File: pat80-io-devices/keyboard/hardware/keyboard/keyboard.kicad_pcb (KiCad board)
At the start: 2 copper layers, 117 parts, among them J3 Keyboard connector, SW1 1, SW10 3, SW11 E, SW12 D, SW13 C, SW14 V, SW15 F, SW16 R, SW17 4, SW18 5, SW19 T, SW2 Q, SW20 G, SW21 B, SW22 N, SW23 H, SW24 Y, SW25 6, SW26 7, SW27 U, SW28 J, SW29 M, SW3 A, SW30 ', SW31 K, SW32 I, SW33 8, SW34 9, SW35 O, SW36 L, SW37 P, SW38 [, SW39 ], SW4 Z, SW40 0, SW41 BACKSPACE, SW42 TILDE, SW43 TAB, SW44 ,, SW45 ., SW46 SPACE, SW47 /, SW48 ;, SW49 LSHIFT, SW5 X, SW50 CTRL, SW51 RSHIFT, SW52 RETURN, SW53 PATO, SW54 CAPSLK, SW6 S, SW7 W, SW8 2, SW9 CAPSLK_LED

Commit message: Fine-positioned caps lock switch
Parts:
- removed SW9: CAPSLK_LED, footprints:SW_TH_DPDT_Pushbutton_Latched
- moved R2 115.5 mm to (151.1, 20.3), turned to 90 degrees
- moved D9 39.0 mm to (34.3, 94.5), turned to 180 degrees
- moved R1 19.2 mm to (29.2, 71.1), turned to 270 degrees
- moved SW54 13.5 mm to (37.5, 69.2)
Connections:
- SW54 pad 4: (no net) -> Net-(SW54-Pad4)
- SW54 pad 5: (no net) -> GND
- SW54 pad 6: (no net) -> Net-(D9-Pad1)
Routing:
- net /ROW0: track 181.7 -> 5.46 mm
- net VCC: track 46.6 -> 50.1 mm

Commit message: Distanced keys to avoid interference
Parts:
- moved D51 8.47 mm to (252.1, 69.2)
- moved SW52 8.47 mm to (260.6, 72.0)
- moved D39 8.18 mm to (271.0, 47.9)
- moved SW39 8.18 mm to (279.5, 51.7)
- moved D36 7.85 mm to (219.7, 69.2)
- moved SW36 7.85 mm to (228.7, 72.0)
- moved SW50 7.69 mm to (226.9, 112.8)
- moved D49 7.69 mm to (218.7, 109.3)
- moved D38 7.67 mm to (251.5, 47.9)
- moved SW38 7.67 mm to (259.7, 51.7)
- moved D31 7.24 mm to (200.0, 69.2)
- moved SW31 7.24 mm to (208.8, 72.0)
- moved SW37 7.17 mm to (239.9, 51.7)
- moved D37 7.17 mm to (230.6, 47.9)
- moved D48 7.15 mm to (193.9, 109.3)
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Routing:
- net /COL0: track 120.8 -> 1.60 mm

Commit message: WIP routing keyboard
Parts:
- SW1, SW10, SW11, SW12, SW13, SW14, SW15, SW16, SW17, SW18, SW19, SW2, SW20, SW21, SW22, SW23, SW24, SW25, SW26, SW27, SW28, SW29, SW3, SW30, SW31, SW32, SW33, SW34, SW35, SW36, SW37, SW38, SW39, SW4, SW40, SW42, SW44, SW45, SW47, SW48, SW5, SW6, SW7, SW8: footprint Button_Switch_Keyboard:SW_Cherry_MX1A_1.00u_PCB -> Button_Switch_Keyboard:SW_Cherry_MX1A_1.00u_Plate
- SW43, SW50, SW53: footprint Button_Switch_Keyboard:SW_Cherry_MX1A_1.50u_PCB -> Button_Switch_Keyboard:SW_Cherry_MX1A_1.50u_Plate
- SW46, SW52: footprint Button_Switch_Keyboard:SW_Cherry_MX1A_2.25u_PCB -> Button_Switch_Keyboard:SW_Cherry_MX1A_2.25u_Plate
- SW49: footprint Button_Switch_Keyboard:SW_Cherry_MX1A_1.25u_PCB -> Button_Switch_Keyboard:SW_Cherry_MX1A_1.25u_Plate
- SW51: footprint Button_Switch_Keyboard:SW_Cherry_MX1A_1.75u_PCB -> Button_Switch_Keyboard:SW_Cherry_MX1A_1.75u_Plate
- moved R2 47.0 mm to (195.6, 5.08)
- moved C5 47.0 mm to (231.1, -1.27)
- moved R3 47.0 mm to (199.4, 5.08)
- moved R4 47.0 mm to (203.2, 5.08)
- moved R5 47.0 mm to (207.0, 5.08)
- moved R6 47.0 mm to (210.8, 5.08)
- moved R7 47.0 mm to (214.6, 5.08)
- moved R8 47.0 mm to (218.4, 5.08)
- moved R9 47.0 mm to (222.2, 5.08)
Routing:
- net /ROW0: track 5.46 -> 201.8 mm
- net /ROW7: track 9.90 -> 199.3 mm
- net /COL1: track 0.00 -> 149.9 mm, vias 0 -> 6
- net /COL2: track 0.00 -> 149.7 mm, vias 0 -> 6
- net /COL0: track 1.60 -> 151.1 mm, vias 0 -> 6
- net VCC: track 50.1 -> 0.36 mm
- net GND: track 60.3 -> 40.6 mm
- net /ROW6: track 7.88 -> 0.00 mm
- net /ROW5: track 6.61 -> 0.51 mm
- net /ROW3: track 5.26 -> 0.00 mm
- net /ROW4: track 5.79 -> 0.76 mm
- net /ROW2: track 4.74 -> 0.00 mm
- net /ROW1: track 4.68 -> 0.61 mm
- net Net-(D1-Pad2): track 0.00 -> 3.82 mm

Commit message: WIP routing keyboard
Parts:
- moved J3 5.39 mm to (126.0, 12.2)
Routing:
- net /COL6: track 0.00 -> 470.9 mm
- net /ROW1: track 0.61 -> 381.5 mm
- net /COL4: track 0.00 -> 294.2 mm, vias 0 -> 4
- net Net-(D50-Pad2): track 0.00 -> 283.5 mm
- net /COL5: track 0.25 -> 258.3 mm, vias 0 -> 2
- net /ROW2: track 0.00 -> 225.6 mm
- net GND: track 40.6 -> 261.1 mm
- net /ROW3: track 0.00 -> 211.2 mm
- net /COL3: track 0.00 -> 195.4 mm, vias 0 -> 6
- net VCC: track 0.36 -> 181.2 mm, vias 0 -> 2
- net /ROW6: track 0.00 -> 125.1 mm
- net /ROW5: track 0.51 -> 125.5 mm
- net /ROW4: track 0.76 -> 125.8 mm
- net /COL0: track 151.1 -> 222.2 mm
- net /COL1: track 149.9 -> 182.9 mm
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
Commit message: WIP routing keyboard
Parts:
- moved R3 106.2 mm to (286.4, 66.0), turned to 180 degrees
- moved R5 106.0 mm to (281.9, 80.0)
- moved R7 81.2 mm to (287.0, 41.9), turned to 180 degrees
- moved C5 77.5 mm to (308.6, -2.54)
- moved R4 77.5 mm to (280.7, 3.81)
- moved R9 77.5 mm to (299.7, 3.81)
- moved R2 77.5 mm to (273.1, 3.81), turned to 180 degrees
- moved R6 76.2 mm to (284.5, 24.8), turned to 270 degrees
- moved R8 14.0 mm to (232.4, 5.08), turned to 180 degrees
- moved J3 9.65 mm to (126.0, 2.54)
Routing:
- net /ROW4: track 125.8 -> 595.3 mm, vias 0 -> 6
- net /ROW3: track 211.2 -> 573.5 mm, vias 0 -> 2
- net /ROW5: track 125.5 -> 370.3 mm, vias 0 -> 4
- net /ROW2: track 225.6 -> 424.9 mm, vias 0 -> 4
- net /ROW6: track 125.1 -> 267.7 mm, vias 0 -> 2
- net /ROW1: track 381.5 -> 467.9 mm, vias 0 -> 2
- net /ROW7: track 199.3 -> 244.8 mm, vias 0 -> 2
- net /ROW0: track 201.8 -> 234.4 mm, vias 0 -> 2
- net VCC: track 181.2 -> 153.3 mm, vias 2 -> 1
- net GND: track 261.1 -> 271.8 mm
- net /COL5: track 258.3 -> 268.0 mm
- net /COL3: track 195.4 -> 205.1 mm
- net /COL1: track 182.9 -> 192.5 mm
- net /COL0: track 222.2 -> 231.9 mm
- net /COL6: track 470.9 -> 480.6 mm
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
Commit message: Completed routing keyboard PCB
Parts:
- R1, R6, R7, R8: footprint Resistor_THT:R_Axial_DIN0207_L6.3mm_D2.5mm_P7.62mm_Horizontal -> Resistor_THT:R_Axial_DIN0207_L6.3mm_D2.5mm_P10.16mm_Horizontal
- R9: footprint Resistor_THT:R_Axial_DIN0207_L6.3mm_D2.5mm_P7.62mm_Horizontal -> Resistor_THT:R_Axial_DIN0207_L6.3mm_D2.5mm_P15.24mm_Horizontal
- moved C5 197.6 mm to (114.9, 36.8)
- moved R3 141.5 mm to (146.7, 43.8), turned to 90 degrees
- moved R4 136.8 mm to (149.9, 43.8)
- moved R2 135.6 mm to (143.5, 43.8), turned to 90 degrees
- moved R5 125.7 mm to (161.9, 42.5)
- moved R6 118.4 mm to (167.6, 43.8), turned to 90 degrees
- moved R7 113.7 mm to (173.4, 41.9), turned to 90 degrees
- moved R9 111.0 mm to (196.2, 43.8), turned to 270 degrees
- moved R8 63.2 mm to (179.7, 40.0), turned to 90 degrees
- moved D46 25.9 mm to (136.8, 134.7)
- moved D47 25.9 mm to (169.2, 134.7)
- moved D48 25.9 mm to (188.8, 134.7)
- moved D44 25.9 mm to (84.7, 134.7)
- moved D45 25.9 mm to (104.4, 134.7)
- moved D49 25.9 mm to (213.6, 134.7)
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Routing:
- net /ROW6: track 267.7 -> 535.3 mm, vias 2 -> 4
- net VCC: track 153.3 -> 312.8 mm, vias 1 -> 2
- net /COL5: track 268.0 -> 377.1 mm, vias 2 -> 4
- net /ROW0: track 234.4 -> 333.9 mm, vias 2 -> 4
- net /ROW3: track 573.5 -> 622.7 mm, vias 2 -> 4
- net /ROW5: track 370.3 -> 411.3 mm, vias 4 -> 6
- net /ROW4: track 595.3 -> 589.8 mm
- net GND: track 271.8 -> 275.3 mm
- net /ROW7: track 244.8 -> 244.0 mm

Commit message: Keyboard PCB: edge cuts and mounting holes
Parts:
- added REF**: MountingHole_4.3mm_M4, MountingHole:MountingHole_4.3mm_M4, F.Cu at (205.7, 43.2)
- added REF**: MountingHole_4.3mm_M4, MountingHole:MountingHole_4.3mm_M4, F.Cu at (49.5, 137.2)
- added REF**: MountingHole_4.3mm_M4, MountingHole:MountingHole_4.3mm_M4, F.Cu at (154.9, 141.0)
- added REF**: MountingHole_4.3mm_M4, MountingHole:MountingHole_4.3mm_M4, F.Cu at (250.2, 123.2)
- added REF**: MountingHole_4.3mm_M4, MountingHole:MountingHole_4.3mm_M4, F.Cu at (25.4, 35.6)
- added REF**: MountingHole_4.3mm_M4, MountingHole:MountingHole_4.3mm_M4, F.Cu at (104.1, 35.6)
- added REF**: MountingHole_4.3mm_M4, MountingHole:MountingHole_4.3mm_M4, F.Cu at (269.2, 64.8)
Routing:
- net VCC: track 312.8 -> 253.2 mm
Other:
- board outline added: 273.1 x 144.8 mm
- board text added: "PAT80 Keyboard"
- board text added: "ver 1.0"

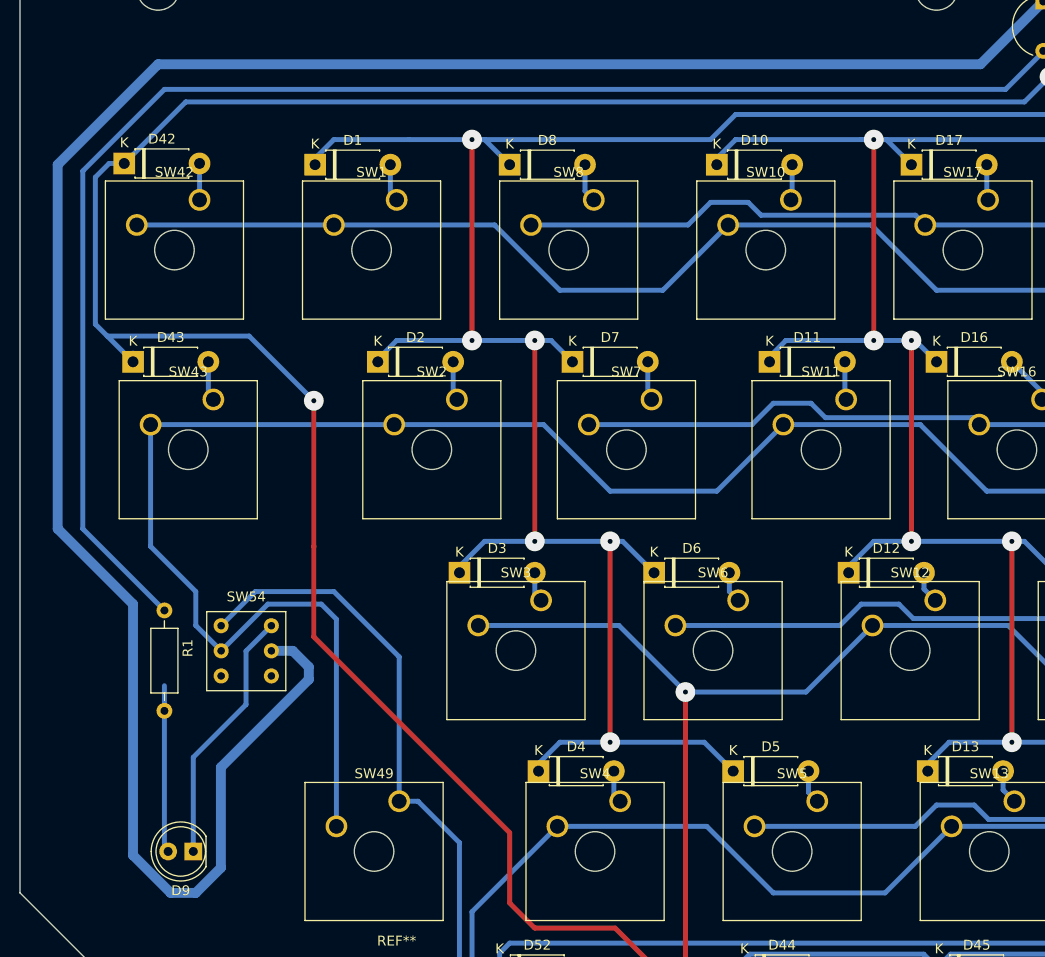
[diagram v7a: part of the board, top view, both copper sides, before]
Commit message: Fixed caps lock footprint error
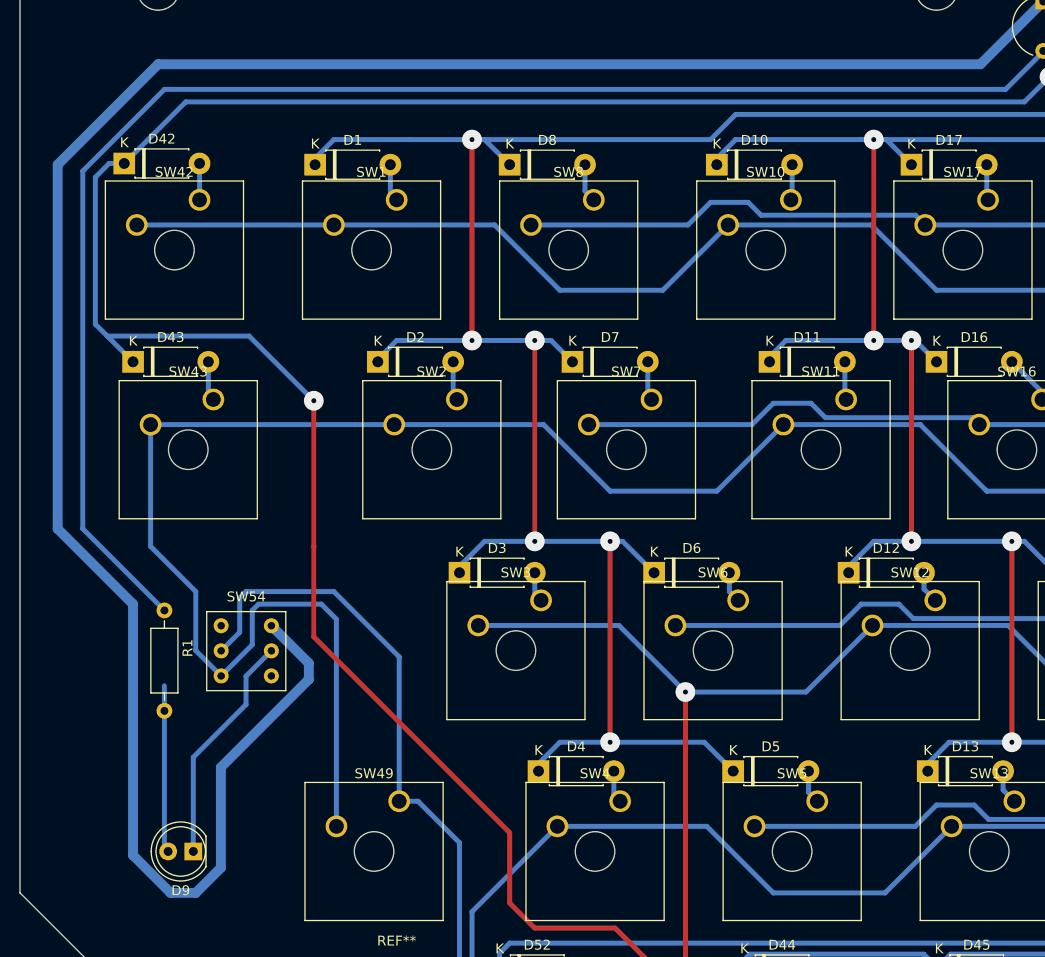
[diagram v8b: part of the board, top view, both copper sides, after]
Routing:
- net /ROW1: track 468.1 -> 473.7 mm
- net Net-(D50-Pad2): track 283.5 -> 286.5 mm
- net Net-(D9-Pad1): track 26.1 -> 23.6 mm
- net GND: track 275.3 -> 276.6 mm
